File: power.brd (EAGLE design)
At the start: 50 x 25 mm, 21 parts, among them CON1 4UCON-19963, CON2 4UCON-19836, CON3 4UCON-10709, CON4 4UCON-10709, IC1 TPS62133, SW1 SWITCHSWITCH

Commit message: Updated everything
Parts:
- JP1, JP2: value (none) -> EXT; device pinhead:1X02 -> robopoly:EXT
- moved CON2 1.50 mm to (0.00, 17.5)
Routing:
- net 5V/3A: track 100.0 -> 97.4 mm
- net VCC: track 79.6 -> 80.3 mm
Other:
- outline, holes or cut-outs redrawn
- board text added: "Pagnamenta & Kangur - 2014"
- board text added: "Ver. 2"
- board text removed: "Pagnamenta & Kangur - 2013"
- board text removed: "Ver. 1"
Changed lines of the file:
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@@
 <?xml version="1.0" encoding="utf-8"?>
 <!DOCTYPE eagle SYSTEM "eagle.dtd">
-<eagle version="6.4">
+<eagle version="6.5.0">
 <drawing>
 <settings>
@@
 <setting verticaltext="up"/>
 </settings>
-<grid distance="1" unitdist="mm" unit="mm" style="lines" multiple="1" display="yes" altdistance="0.25" altunitdist="mm" altunit="mm"/>
+<grid distance="1" unitdist="mm" unit="mm" style="lines" multiple="1" display="yes" altdistance="0.5" altunitdist="mm" altunit="mm"/>
 <layers>
 <layer number="1" name="Top" color="4" fill="1" visible="yes" active="yes"/>
@@
 <layer number="27" name="tValues" color="7" fill="1" visible="no" active="yes"/>
 <layer number="28" name="bValues" color="7" fill="1" visible="no" active="yes"/>
-<layer number="29" name="tStop" color="7" fill="3" visible="yes" active="yes"/>
-<layer number="30" name="bStop" color="7" fill="6" visible="yes" active="yes"/>
+<layer number="29" name="tStop" color="7" fill="3" visible="no" active="yes"/>
+<layer number="30" name="bStop" color="7" fill="6" visible="no" active="yes"/>
 <layer number="31" name="tCream" color="7" fill="4" visible="no" active="yes"/>
 <layer number="32" name="bCream" color="7" fill="5" visible="no" active="yes"/>
@@
 <board>
 <plain>
-<wire x1="0" y1="0" x2="50" y2="0" width="0" layer="20"/>
-<wire x1="50" y1="0" x2="50" y2="25" width="0" layer="20"/>
-<wire x1="50" y1="25" x2="0" y2="25" width="0" layer="20"/>
-<wire x1="0" y1="25" x2="0" y2="0" width="0" layer="20"/>
-<dimension x1="50" y1="25" x2="0" y2="25" x3="25" y3="30" textsize="1.778" layer="48"/>
-<dimension x1="0" y1="25" x2="0" y2="0" x3="-5" y3="12.5" textsize="1.778" layer="48"/>
-<text x="6" y="15.5" size="1.27" layer="21" font="vector" ratio="12" align="center-right">GND</text>
-<text x="6" y="19" size="1.27" layer="21" font="vector" ratio="12" align="center-right">5V</text>
-<text x="6" y="22.5" size="1.27" layer="21" font="vector" ratio="12" align="center-right">VB</text>
+<wire x1="0" y1="23.73" x2="0" y2="1.27" width="0" layer="20"/>
+<wire x1="0" y1="1.27" x2="1.27" y2="0" width="0" layer="20" curve="90"/>
+<wire x1="1.27" y1="0" x2="48.73" y2="0" width="0" layer="20"/>
+<wire x1="48.73" y1="0" x2="50" y2="1.27" width="0" layer="20" curve="90"/>
+<wire x1="50" y1="1.27" x2="50" y2="23.73" width="0" layer="20"/>
+<wire x1="50" y1="23.73" x2="48.73" y2="25" width="0" layer="20" curve="90"/>
+<wire x1="48.73" y1="25" x2="1.27" y2="25" width="0" layer="20"/>
+<wire x1="1.27" y1="25" x2="0" y2="23.73" width="0" layer="20" curve="90"/>
+<dimension x1="50" y1="25" x2="0" y2="25" x3="25" y3="35" textsize="1.778" layer="48"/>
+<dimension x1="0" y1="25" x2="0" y2="0" x3="-10" y3="12.5" textsize="1.778" layer="48"/>
+<text x="6" y="14" size="1.27" layer="21" font="vector" ratio="12" align="center-right">GND</text>
+<text x="6" y="17.5" size="1.27" layer="21" font="vector" ratio="12" align="center-right">5V</text>
+<text x="6" y="21" size="1.27" layer="21" font="vector" ratio="12" align="center-right">VB</text>
 <text x="30" y="11" size="1.27" layer="21" font="vector" ratio="12" rot="R180" align="bottom-center">C1</text>
 <text x="34" y="11" size="1.27" layer="21" font="vector" ratio="12" rot="R180" align="bottom-center">C2</text>
@@
 <text x="38" y="11" size="1.27" layer="21" font="vector" ratio="12" rot="R180" align="bottom-center">R2</text>
 <text x="47.5" y="13" size="1.27" layer="21" font="vector" ratio="12" rot="R270" align="bottom-center">PWR</text>
-<text x="2" y="1" size="1.27" layer="22" font="vector" ratio="12" rot="MR0" align="bottom-right">Pagnamenta &amp; Kangur - 2013</text>
-<text x="6" y="19" size="1.27" layer="22" font="vector" ratio="12" rot="MR180" align="center-right">5V</text>
-<text x="6" y="15.5" size="1.27" layer="22" font="vector" ratio="12" rot="MR180" align="center-right">GND</text>
-<text x="6" y="22.5" size="1.27" layer="22" font="vector" ratio="12" rot="MR180" align="center-right">VB</text>
-<text x="6" y="9" size="1.27" layer="16" font="vector" ratio="12" rot="MR180" align="center-left">Ver. 1</text>
+<text x="2" y="1" size="1.27" layer="22" font="vector" ratio="12" rot="MR0" align="bottom-right">Pagnamenta &amp; Kangur - 2014</text>
+<text x="6" y="17.5" size="1.27" layer="22" font="vector" ratio="12" rot="MR180" align="center-right">5V</text>
+<text x="6" y="14" size="1.27" layer="22" font="vector" ratio="12" rot="MR180" align="center-right">GND</text>
+<text x="6" y="21" size="1.27" layer="22" font="vector" ratio="12" rot="MR180" align="center-right">VB</text>
+<text x="6" y="9" size="1.27" layer="16" font="vector" ratio="12" rot="MR180" align="center-left">Ver. 2</text>
 <text x="42" y="18" size="1.27" layer="21" font="vector" ratio="12" rot="R180" align="bottom-center">On</text>
 <text x="47" y="18" size="1.27" layer="21" font="vector" ratio="12" rot="R180" align="bottom-center">Off</text>
-<text x="34" y="18" size="1.27" layer="21" font="vector" ratio="12" rot="R180" align="bottom-center">Switch</text>
+<text x="34" y="19" size="1.27" layer="21" font="vector" ratio="12" rot="R180" align="bottom-center">Switch</text>
 <text x="26" y="16" size="1.778" layer="22" font="vector" ratio="12" rot="MR180" align="center">Power Board</text>
 <text x="42.5" y="6.5" size="1.27" layer="21" font="vector" ratio="12" align="center-right">VB</text>
@@
 <wire x1="0.75" y1="3.5" x2="2.25" y2="3.5" width="0.3048" layer="22"/>
 <text x="44" y="23.5" size="1.27" layer="22" font="vector" ratio="12" rot="MR180" align="center">17V max.</text>
+<dimension x1="15" y1="25" x2="35" y2="25" x3="25" y3="30" textsize="1.778" layer="48"/>
+<dimension x1="0" y1="5" x2="0" y2="20" x3="-5" y3="12.5" textsize="1.778" layer="48"/>
 </plain>
 <attributes>
@@
 <element name="H1" library="robopoly" package="3,2-PAD" value="MOUNT-PAD-ROUND3.2" x="35" y="5"/>
 <element name="H2" library="robopoly" package="3,2-PAD" value="MOUNT-PAD-ROUND3.2" x="15" y="20"/>
-<element name="CON2" library="karl_new" package="4UCON-19836" value="4UCON-19836" x="0" y="19" rot="R270"/>
+<element name="CON2" library="karl_new" package="4UCON-19836" value="4UCON-19836" x="0" y="17.5" rot="R270"/>
 <element name="CON1" library="karl_new" package="4UCON-19963" value="4UCON-19963" x="50" y="5" rot="R90"/>
 <element name="C1" library="rcl" package="C0805" value="10uF" x="30" y="13" rot="R270"/>
@@
 <element name="U$10" library="robopoly" package="OPEN-HARDWARE-BOTTOM-SMALL" value="OPEN-HARDWARE-LOGOBOTTOM-SMALL" x="46.4" y="16.5"/>
 <element name="SW1" library="karl_new" package="SWITCH" value="SWITCHSWITCH" x="44" y="21"/>
-<element name="JP1" library="pinhead" package="1X02" value="" x="34" y="21" rot="R180"/>
-<element name="JP2" library="pinhead" package="1X02" value="" x="42" y="13" rot="R270"/>
+<element name="JP1" library="robopoly" package="EXT" value="EXT" x="34" y="21" rot="R180"/>
+<element name="JP2" library="robopoly" package="EXT" value="EXT" x="42" y="13" rot="R270"/>
 <element name="LICENCE1" library="robopoly" package="CREATIVE-COMMONS" value="LICENCECC-BOTTOM" x="46.4" y="10.5"/>
 </elements>
@@
 <contactref element="H2" pad="B3,2"/>
 <polygon width="0.4064" layer="1" isolate="0.4064" rank="6">
-<vertex x="0" y="25"/>
-<vertex x="50" y="25"/>
-<vertex x="50" y="0"/>
-<vertex x="0" y="0"/>
+<vertex x="1.27" y="25"/>
+<vertex x="48.73" y="25" curve="-90"/>
+<vertex x="50" y="23.73"/>
+<vertex x="50" y="1.27" curve="-90"/>
+<vertex x="48.73" y="0"/>
+<vertex x="1.27" y="0" curve="-90"/>
+<vertex x="0" y="1.27"/>
+<vertex x="0" y="23.73" curve="-90"/>
 </polygon>
 <polygon width="0.4064" layer="16" isolate="0.4064" rank="6">
-<vertex x="0" y="25"/>
-<vertex x="50" y="25"/>
-<vertex x="50" y="0"/>
-<vertex x="0" y="0"/>
+<vertex x="1.27" y="25"/>
+<vertex x="48.73" y="25" curve="-90"/>
+<vertex x="50" y="23.73"/>
+<vertex x="50" y="1.27" curve="-90"/>
+<vertex x="48.73" y="0"/>
+<vertex x="1.27" y="0" curve="-90"/>
+<vertex x="0" y="1.27"/>
+<vertex x="0" y="23.73" curve="-90"/>
 </polygon>
 <contactref element="C1" pad="2"/>
@@
 <wire x1="32.73" y1="21" x2="29.73" y2="24" width="1.27" layer="16"/>
 <contactref element="CON2" pad="1"/>
-<wire x1="29.73" y1="24" x2="9.3" y2="24" width="1.27" layer="16"/>
-<wire x1="9.3" y1="24" x2="7.8" y2="22.5" width="1.27" layer="16"/>
+<wire x1="29.73" y1="24" x2="10.8" y2="24" width="1.27" layer="16"/>
+<wire x1="10.8" y1="24" x2="7.8" y2="21" width="1.27" layer="16"/>
 <wire x1="3.72" y1="6.27" x2="26.58" y2="6.27" width="0.8128" layer="16"/>
 <wire x1="26.7" y1="12.75" x2="26.58" y2="6.27" width="0" layer="19" extent="1-16"/>
@@
 <wire x1="12" y1="13.95" x2="15" y2="13.95" width="1.27" layer="1"/>
 <wire x1="16" y1="13.95" x2="13.88" y2="13.95" width="1.27" layer="1"/>
-<wire x1="12" y1="13.95" x2="7.8" y2="19" width="1.27" layer="1"/>
-<wire x1="7.8" y1="19" x2="3.72" y2="14.92" width="1.016" layer="16"/>
-<wire x1="3.72" y1="14.92" x2="3.72" y2="6.27" width="1.016" layer="16"/>
+<wire x1="12" y1="13.95" x2="7.8" y2="17.5" width="1.27" layer="1"/>
+<wire x1="7.8" y1="17.5" x2="3.72" y2="13.42" width="1.016" layer="16"/>
+<wire x1="3.72" y1="13.42" x2="3.72" y2="6.27" width="1.016" layer="16"/>
 </signal>
 <signal name="PG">

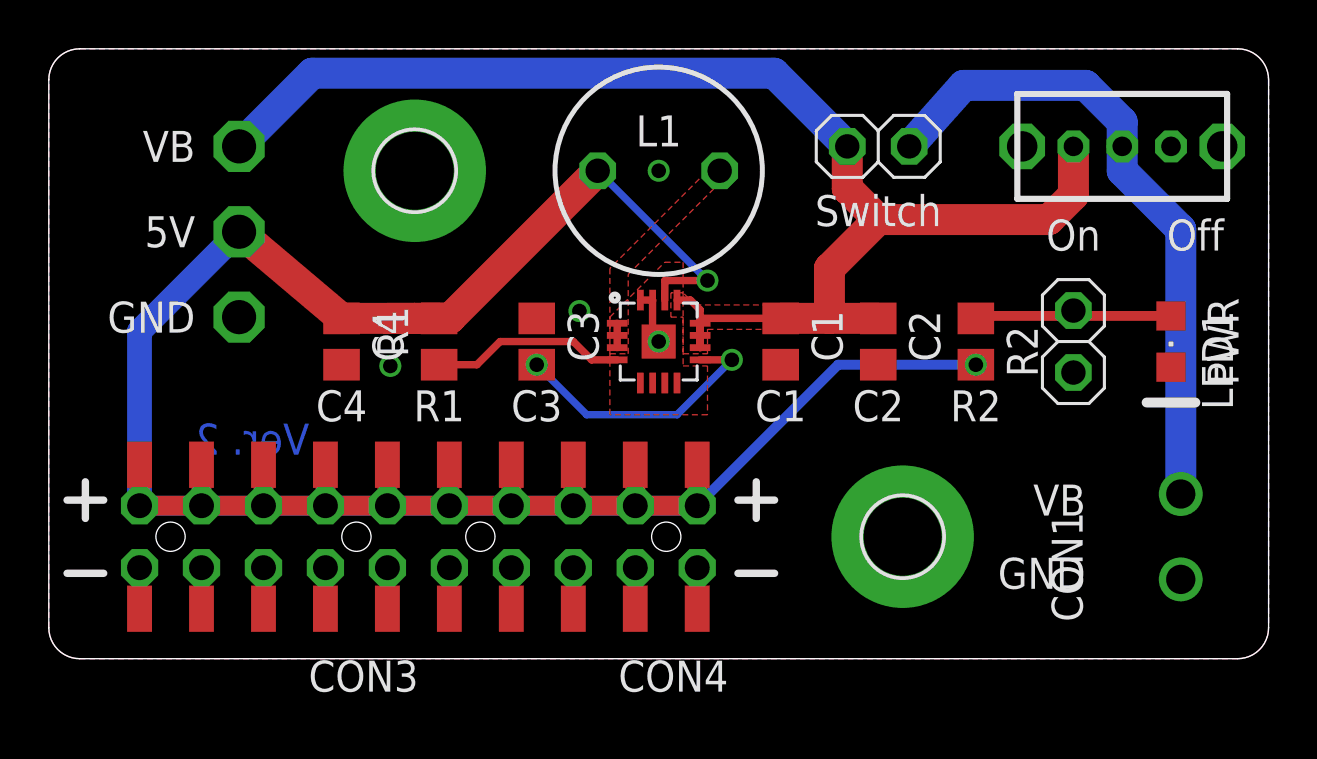
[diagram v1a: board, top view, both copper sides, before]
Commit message: Modified regulator footprint
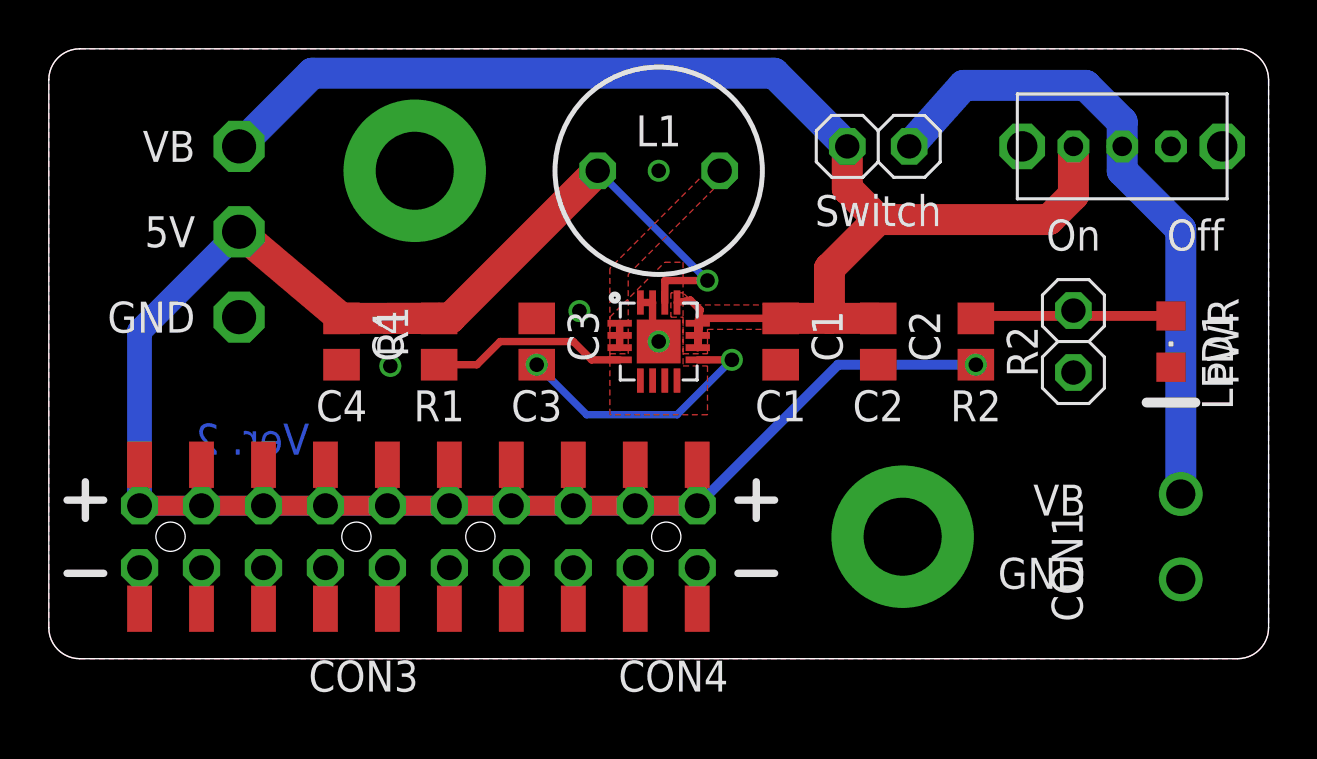
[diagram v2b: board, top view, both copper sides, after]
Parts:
- CON1: device karl_new:4UCON-19963 -> robopoly:4UCON-19963
- CON2: device karl_new:4UCON-19836 -> robopoly:4UCON-19836
- CON3, CON4: device karl_new:4UCON-10709 -> robopoly:4UCON-10709
- L1: device karl_new:09D -> robopoly:09D
- SW1: device karl_new:SWITCH -> robopoly:SWITCH
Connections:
- new net N$1: SW1.3
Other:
- board text added: "2014-02-23"
- board text added: "Licence: Creative Commons"
- board text added: "Version: 2"
- board text added: "http://robopoly.epfl.ch"
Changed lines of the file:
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@@
 <layer number="27" name="tValues" color="7" fill="1" visible="no" active="yes"/>
 <layer number="28" name="bValues" color="7" fill="1" visible="no" active="yes"/>
-<layer number="29" name="tStop" color="7" fill="3" visible="no" active="yes"/>
+<layer number="29" name="tStop" color="7" fill="3" visible="yes" active="yes"/>
 <layer number="30" name="bStop" color="7" fill="6" visible="no" active="yes"/>
 <layer number="31" name="tCream" color="7" fill="4" visible="no" active="yes"/>
@@
 <layer number="220" name="220bmp" color="21" fill="1" visible="no" active="no"/>
 <layer number="221" name="221bmp" color="22" fill="1" visible="no" active="no"/>
+<layer number="222" name="222bmp" color="23" fill="1" visible="no" active="no"/>
 <layer number="223" name="223bmp" color="24" fill="1" visible="no" active="no"/>
 <layer number="224" name="224bmp" color="25" fill="1" visible="no" active="no"/>
@@
 <dimension x1="15" y1="25" x2="35" y2="25" x3="25" y3="30" textsize="1.778" layer="48"/>
 <dimension x1="0" y1="5" x2="0" y2="20" x3="-5" y3="12.5" textsize="1.778" layer="48"/>
+<text x="0" y="-3" size="1.778" layer="48" font="vector" ratio="12">Power Board</text>
+<text x="50" y="-3" size="1.778" layer="48" font="vector" ratio="12" align="bottom-right">Version: 2</text>
+<text x="50" y="-6" size="1.27" layer="48" font="vector" ratio="12" align="bottom-right">2014-02-23</text>
+<text x="0" y="-6" size="1.27" layer="48" font="vector" ratio="12">http://robopoly.epfl.ch</text>
+<text x="0" y="-9" size="1.27" layer="48" font="vector" ratio="12">Licence: Creative Commons</text>
 </plain>
 <attributes>
@@
 <element name="H1" library="robopoly" package="3,2-PAD" value="MOUNT-PAD-ROUND3.2" x="35" y="5"/>
 <element name="H2" library="robopoly" package="3,2-PAD" value="MOUNT-PAD-ROUND3.2" x="15" y="20"/>
-<element name="CON2" library="karl_new" package="4UCON-19836" value="4UCON-19836" x="0" y="17.5" rot="R270"/>
-<element name="CON1" library="karl_new" package="4UCON-19963" value="4UCON-19963" x="50" y="5" rot="R90"/>
+<element name="CON2" library="robopoly" package="4UCON-19836" value="4UCON-19836" x="0" y="17.5" rot="R270"/>
+<element name="CON1" library="robopoly" package="4UCON-19963" value="4UCON-19963" x="50" y="5" rot="R90"/>
 <element name="C1" library="rcl" package="C0805" value="10uF" x="30" y="13" rot="R270"/>
 <element name="C2" library="rcl" package="C0805" value="100nF" x="34" y="13" rot="R270"/>
 <element name="C3" library="rcl" package="C0805" value="3.3nF" x="20" y="13" rot="R270"/>
 <element name="C4" library="rcl" package="C0805" value="22uF" x="12" y="13" rot="R270"/>
-<element name="L1" library="karl_new" package="09D" value="2.2uH" x="25" y="20" rot="R180"/>
+<element name="L1" library="robopoly" package="09D" value="2.2uH" x="25" y="20" rot="R180"/>
 <element name="R1" library="rcl" package="R0805" value="100K" x="16" y="13" rot="R90"/>
 <element name="R2" library="rcl" package="R0805" value="1K" x="38" y="13" rot="R270"/>
 <element name="LED1" library="led" package="CHIPLED_0805" value="" x="46" y="13" rot="R180"/>
-<element name="CON3" library="karl_new" package="4UCON-10709" value="4UCON-10709" x="8.8" y="5" rot="R180"/>
-<element name="CON4" library="karl_new" package="4UCON-10709" value="4UCON-10709" x="21.5" y="5" rot="R180"/>
+<element name="CON3" library="robopoly" package="4UCON-10709" value="4UCON-10709" x="8.8" y="5" rot="R180"/>
+<element name="CON4" library="robopoly" package="4UCON-10709" value="4UCON-10709" x="21.5" y="5" rot="R180"/>
 <element name="U$9" library="robopoly" package="ROBOPOLY-LOGO-BOTTOM-BIG" value="ROBOPOLY-LOGOBOTTOM-BIG" x="25" y="10"/>
 <element name="U$10" library="robopoly" package="OPEN-HARDWARE-BOTTOM-SMALL" value="OPEN-HARDWARE-LOGOBOTTOM-SMALL" x="46.4" y="16.5"/>
-<element name="SW1" library="karl_new" package="SWITCH" value="SWITCHSWITCH" x="44" y="21"/>
+<element name="SW1" library="robopoly" package="SWITCH" value="SWITCHSWITCH" x="44" y="21"/>
 <element name="JP1" library="robopoly" package="EXT" value="EXT" x="34" y="21" rot="R180"/>
 <element name="JP2" library="robopoly" package="EXT" value="EXT" x="42" y="13" rot="R270"/>
@@
 <contactref element="JP2" pad="2"/>
 <contactref element="C3" pad="1"/>
-<wire x1="24.25" y1="14.7" x2="24.75" y2="14.7" width="0.3048" layer="1"/>
-<wire x1="24.75" y1="14.7" x2="24.75" y2="13.25" width="0.3048" layer="1"/>
+<wire x1="24.25" y1="14.6" x2="24.75" y2="14.6" width="0.3048" layer="1"/>
+<wire x1="24.75" y1="14.6" x2="24.75" y2="13.25" width="0.3048" layer="1"/>
 <wire x1="24.75" y1="13.25" x2="25" y2="13" width="0.3048" layer="1"/>
 <polygon width="0.4064" layer="1" thermals="no" rank="2">
@@
 <contactref element="SW1" pad="1"/>
 <contactref element="JP1" pad="2"/>
-<wire x1="25.75" y1="14.7" x2="26.3" y2="14.7" width="0.3048" layer="1"/>
+<wire x1="25.75" y1="14.6" x2="26.3" y2="14.7" width="0.3048" layer="1"/>
 <wire x1="26.3" y1="14.7" x2="26.7" y2="14.3" width="0.3048" layer="1"/>
-<wire x1="26.7" y1="14.3" x2="26.7" y2="13.75" width="0.3048" layer="1"/>
-<wire x1="26.7" y1="13.75" x2="26.7" y2="13.25" width="0.3048" layer="1"/>
-<wire x1="26.7" y1="13.25" x2="26.7" y2="12.75" width="0.3048" layer="1"/>
+<wire x1="26.7" y1="14.3" x2="26.6" y2="13.75" width="0.3048" layer="1"/>
+<wire x1="26.6" y1="13.75" x2="26.6" y2="13.25" width="0.3048" layer="1"/>
+<wire x1="26.6" y1="13.25" x2="26.6" y2="12.75" width="0.3048" layer="1"/>
 <wire x1="30" y1="13.95" x2="26.7" y2="13.95" width="0.3048" layer="1"/>
-<wire x1="26.7" y1="13.95" x2="26.7" y2="12.75" width="0.3048" layer="1"/>
+<wire x1="26.7" y1="13.95" x2="26.6" y2="12.75" width="0.3048" layer="1"/>
 <wire x1="30" y1="13.95" x2="32" y2="13.95" width="1.27" layer="1"/>
 <wire x1="32" y1="13.95" x2="34" y2="13.95" width="1.27" layer="1"/>
@@
 <wire x1="10.8" y1="24" x2="7.8" y2="21" width="1.27" layer="16"/>
 <wire x1="3.72" y1="6.27" x2="26.58" y2="6.27" width="0.8128" layer="16"/>
-<wire x1="26.7" y1="12.75" x2="26.58" y2="6.27" width="0" layer="19" extent="1-16"/>
+<wire x1="26.6" y1="12.75" x2="26.58" y2="6.27" width="0" layer="19" extent="1-16"/>
 </signal>
 <signal name="SS/TR">
 <contactref element="IC1" pad="9"/>
 <contactref element="C3" pad="2"/>
-<wire x1="26.7" y1="12.25" x2="28" y2="12.25" width="0.3048" layer="1"/>
+<wire x1="26.6" y1="12.25" x2="28" y2="12.25" width="0.3048" layer="1"/>
 <via x="28" y="12.25" extent="1-16" drill="0.6" shape="octagon"/>
 <via x="20" y="12.05" extent="1-16" drill="0.6" shape="octagon"/>
@@
 <wire x1="26.58" y1="7.95" x2="26.58" y2="6.27" width="0.8128" layer="1"/>
 <wire x1="26.58" y1="6.27" x2="24.04" y2="6.27" width="0.8128" layer="1"/>
-<wire x1="25.25" y1="14.7" x2="25.25" y2="15.5" width="0.3048" layer="1"/>
+<wire x1="25.25" y1="14.6" x2="25.25" y2="15.5" width="0.3048" layer="1"/>
 <wire x1="25.25" y1="15.5" x2="27" y2="15.5" width="0.3048" layer="1"/>
 <wire x1="16.45" y1="13.95" x2="16" y2="13.95" width="1.27" layer="1"/>
@@
 <wire x1="18.5" y1="13" x2="21.5" y2="13" width="0.3048" layer="1"/>
 <wire x1="21.5" y1="13" x2="22.25" y2="12.25" width="0.3048" layer="1"/>
-<wire x1="22.25" y1="12.25" x2="23.3" y2="12.25" width="0.3048" layer="1"/>
+<wire x1="22.25" y1="12.25" x2="23.4" y2="12.25" width="0.3048" layer="1"/>
 </signal>
 <signal name="LEDIN">
@@
 <contactref element="IC1" pad="2"/>
 <contactref element="L1" pad="1"/>
-<wire x1="23.3" y1="13.75" x2="23.3" y2="13.25" width="0.3048" layer="1"/>
-<wire x1="23.3" y1="13.25" x2="23.3" y2="12.75" width="0.3048" layer="1"/>
+<wire x1="23.4" y1="13.75" x2="23.4" y2="13.25" width="0.3048" layer="1"/>
+<wire x1="23.4" y1="13.25" x2="23.4" y2="12.75" width="0.3048" layer="1"/>
 <polygon width="0.4064" layer="1" thermals="no">
 <vertex x="23.75" y="12.5"/>
@@
 </polygon>
 </signal>
+<signal name="N$1">
+<contactref element="SW1" pad="3"/>
+</signal>
 </signals>
